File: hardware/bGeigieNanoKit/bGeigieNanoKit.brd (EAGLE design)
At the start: 57.1 x 73.7 mm, 5 parts

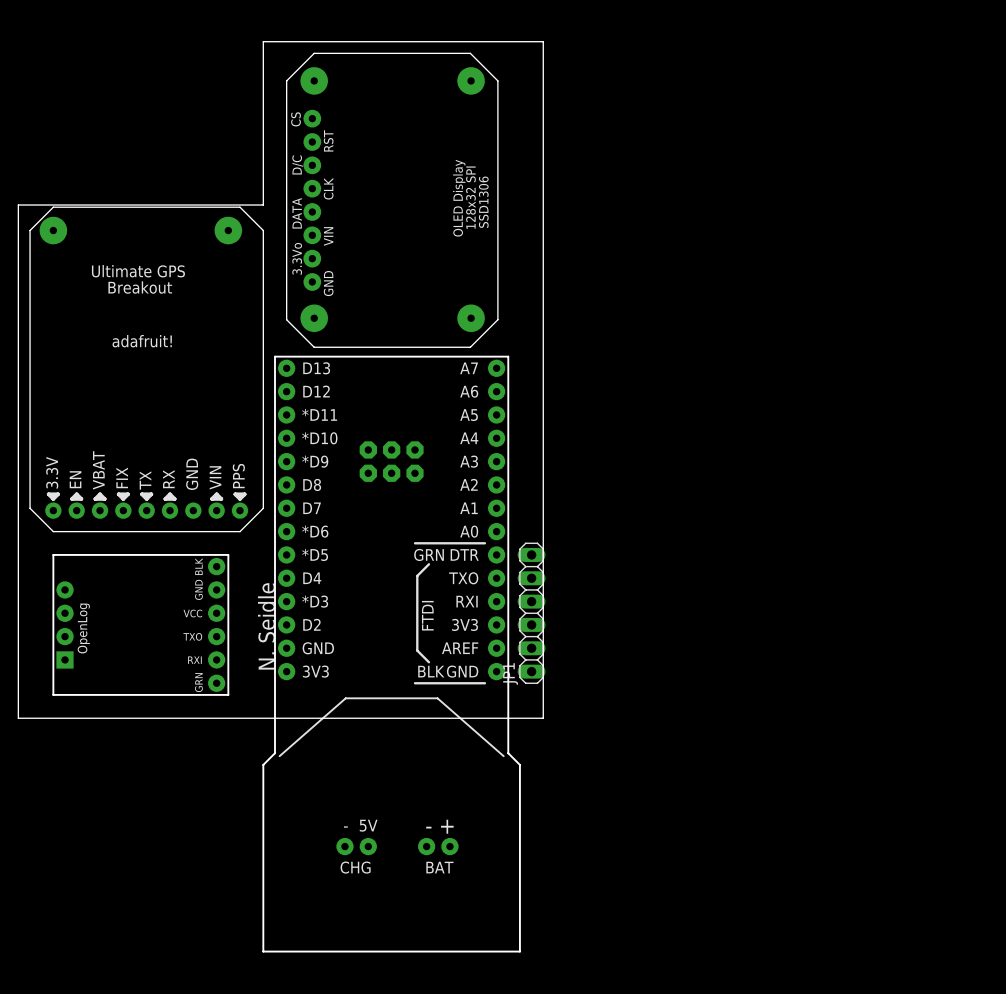
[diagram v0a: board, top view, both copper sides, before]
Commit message: library updated with full module footprints. test components removed. board updated to use new library components.
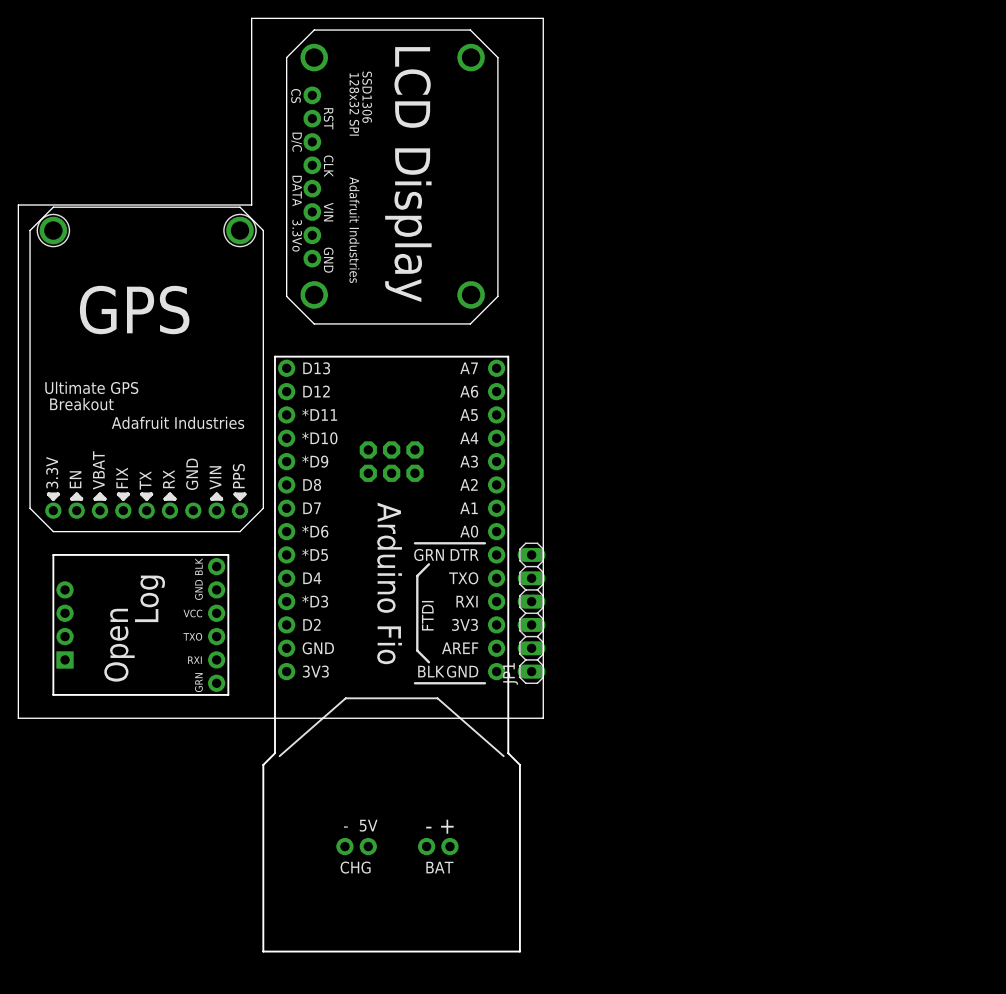
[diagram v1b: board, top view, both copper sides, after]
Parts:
- U$1: value OPENLOGTEST -> OPENLOG; device open_hw_sockets:TEST_OPENLOG -> open_hw_sockets:OPENLOG
- U$2: value FIO_SOCKETTEST -> FIO_SOCKET; device open_hw_sockets:TEST_FIO -> open_hw_sockets:FIO_V23_SOCKET
- U$3: value ULTIMATE_GPSTEST -> ULTIMATE_GPS; device open_hw_sockets:TEST_GPS -> open_hw_sockets:ULTIMATE_GPS_V3
- U$4: value LCD_SOCKETTEST -> SSD1306_128X32_SPI_LCD; device open_hw_sockets:TEST_LCD -> open_hw_sockets:SSD1306_128X32_SPI_LCD
- moved U$4 2.54 mm to (29.2, 100.3)
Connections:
- net GND: now also U$1.JP1$1, U$1.JP1$2, U$3.JP1$3, U$3.U$8$P$1, U$3.U$9$P$1, U$4.JP1$8, U$4.U$2$P$1, U$4.U$3$P$1, U$4.U$4$P$1, U$4.U$5$P$1; no longer U$1.JP1$5, U$1.JP1$6, U$3.JP1$2, U$3.U$8, U$3.U$9, U$4.8, U$4.U$2, U$4.U$3, U$4.U$4, U$4.U$5
- net N$1: now also U$1.JP1$6; no longer U$1.JP1$1
- net N$10: now also U$4.JP1$1; no longer U$4.1
- net N$2: now also U$1.JP1$5; no longer U$1.JP1$2
- net N$3: now also U$1.JP1$4; no longer U$1.JP1$3
- net N$4: now also U$3.JP1$4; no longer U$3.JP1$3
- net N$5: now also U$3.JP1$5; no longer U$3.JP1$4
- net N$6: now also U$4.JP1$5; no longer U$4.5
- net N$7: now also U$4.JP1$4; no longer U$4.4
- net N$8: now also U$4.JP1$3; no longer U$4.3
- net N$9: now also U$4.JP1$2; no longer U$4.2
- net VBAT: now also U$3.JP1$7; no longer U$3.JP1$6
- net VCC: now also U$1.JP1$3, U$3.JP1$9, U$4.JP1$7; no longer U$1.JP1$4, U$3.JP1$8, U$4.7
- net VIN: now also U$3.JP1$2, U$4.JP1$6; no longer U$3.JP1$1, U$4.6
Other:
- board size 57.1 x 73.7 mm -> 57.1 x 76.2 mm

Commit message: updated library footprints with single/double sided options. preliminary component placement on board to verify fit.
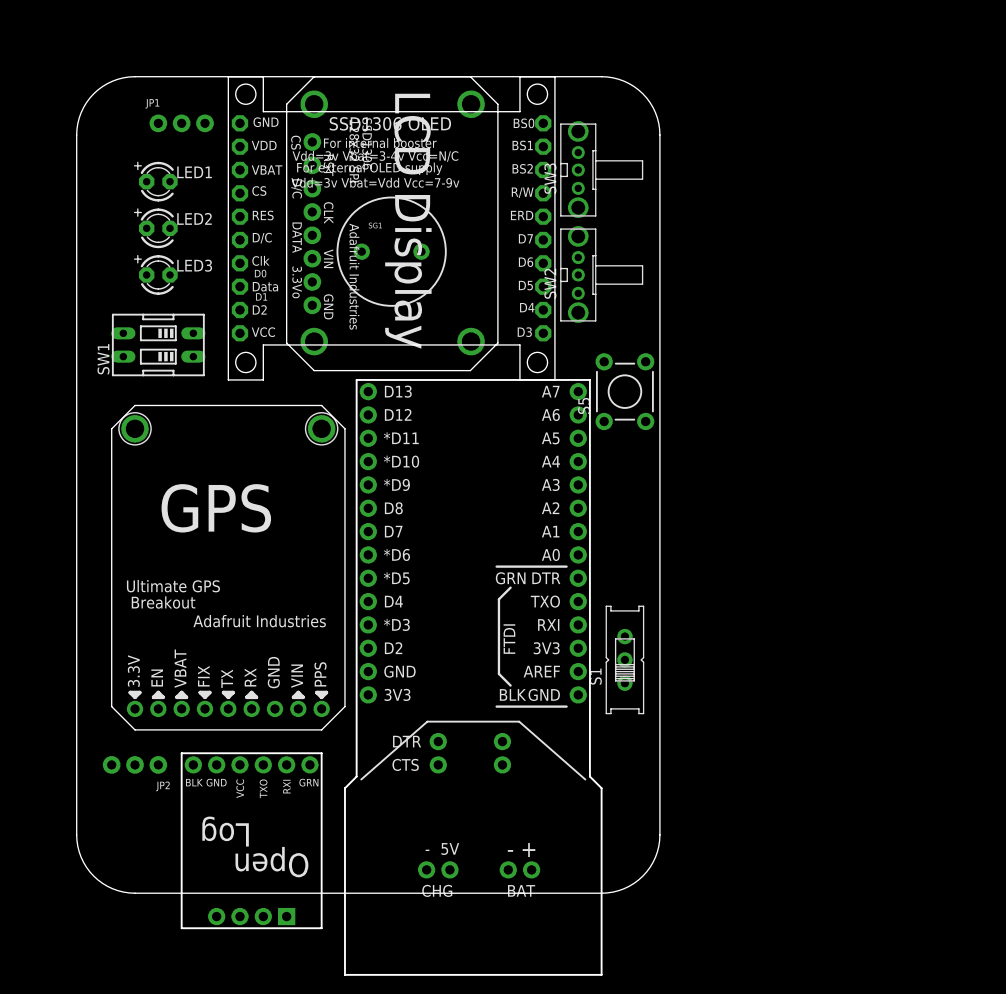
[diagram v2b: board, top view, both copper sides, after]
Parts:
- added JP2: (no value), microbuilder:1X03_ROUND_76
- added LED1, LED2, LED3: (no value), adafruit:LED3MM
- added S1: (no value), adafruit:EG1218
- added S5: (no value), SparkFun:TACTILE-PTH
- added SG1: BUZZERPTH, SparkFun:BUZZER-12MM
- added SW1: (no value), SparkFun:DIPSWITCH-02
- added SW2, SW3: OS102011MA1Q, adafruit:OS102011MA1Q
- added U$5: SSD1306_128X64_LCDTOP, open_hw_sockets:SSD1306_128X64_LCD_TOP
- JP1: device pinhead:1X06 -> microbuilder:1X03_ROUND_76
- U$2: value FIO_SOCKET -> FIO; device open_hw_sockets:FIO_V23_SOCKET -> open_hw_sockets:FIO_SOCKET
- U$3: value ULTIMATE_GPS -> GPS
- U$4: value SSD1306_128X32_SPI_LCD -> LCD
- moved JP1 65.5 mm to (17.8, 90.2), turned to 0 degrees
- moved U$3 23.3 mm to (10.2, 24.1)
- moved U$1 12.0 mm to (33.0, 21.6), turned to 180 degrees
- moved U$2 9.25 mm to (36.8, 62.2)
- moved U$4 5.08 mm to (29.2, 95.2)
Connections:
- removed net N$1: U$1.JP1$6, U$2.JP1$13
- removed net N$10: U$2.JP1$5, U$4.JP1$1
- removed net N$11: JP1.1, U$2.JP5$1
- removed net N$12: JP1.2, U$2.JP5$2
- removed net N$13: JP1.3, U$2.JP5$3
- removed net N$14: JP1.4, U$2.JP5$4
- removed net N$15: JP1.5, U$2.JP5$5
- removed net N$16: JP1.6, U$2.JP5$6
- removed net N$2: U$1.JP1$5, U$2.JP1$12
- removed net N$3: U$1.JP1$4, U$2.JP1$11
- removed net N$4: U$2.JP1$10, U$3.JP1$4
- removed net N$5: U$2.JP1$9, U$3.JP1$5
- removed net N$6: U$2.JP1$7, U$4.JP1$5
- removed net N$7: U$2.JP1$8, U$4.JP1$4
- removed net N$8: U$2.JP1$6, U$4.JP1$3
- removed net N$9: U$2.JP1$4, U$4.JP1$2
- new net 3.3V: U$3.JP1$9, U$4.JP1$7
- new net 3V3: U$2.JP1$1, U$2.JP5$3
- new net VDD: U$5.P0\$2
- net GND: now also U$2.JP5$1, U$5.P0\$1
- net VBAT: now also U$5.P0\$3
- net VCC: now also U$5.P0\$10; no longer U$2.JP1$1, U$3.JP1$9, U$4.JP1$7
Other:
- board size 57.1 x 76.2 mm -> 63.5 x 88.9 mm

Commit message: full set of components added to library. initital placement of all components.
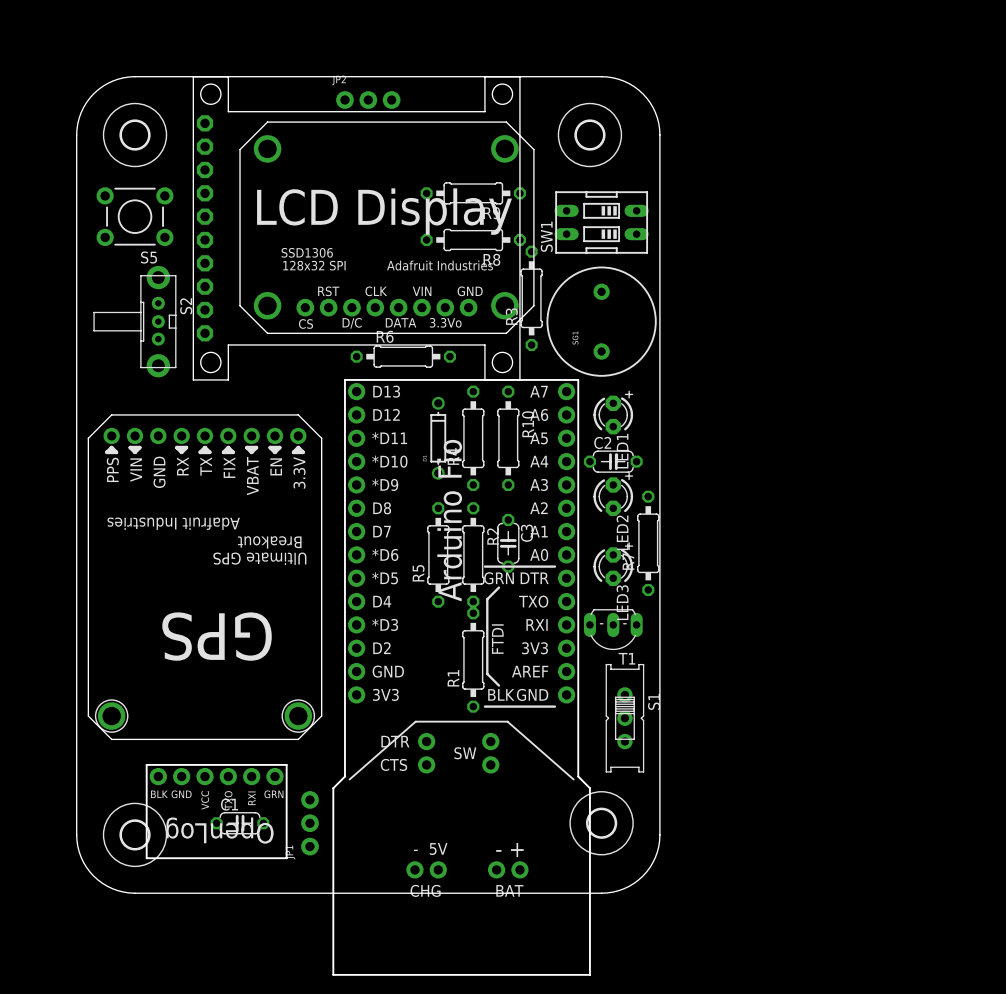
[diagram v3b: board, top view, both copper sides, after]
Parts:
- removed SW2, SW3: OS102011MA1Q, adafruit:OS102011MA1Q
- added C1, C2, C3: (no value), rcl:C050-024X044
- added D1: (no value), adafruit:DO-1N4148
- added H1, H2, H3, H4: MOUNT-HOLE3.0, holes:3,0
- added R1, R10, R2, R3, R4, R5, R6, R7, R8, R9: (no value), rcl:0207/10
- added S2: EG1213, adafruit:EG1213
- added T1: 2SC1815, transistor:TO92-ECB
- LED2: value (none) -> RED
- U$1: value OPENLOG -> OPENLOG_MIN; device open_hw_sockets:OPENLOG -> open_hw_sockets:OPENLOG_MIN
- U$2: value FIO -> FIO_SOCKETBOT; device open_hw_sockets:FIO_SOCKET -> open_hw_sockets:FIO_V23_SOCKET_BOT
- U$5: value SSD1306_128X64_LCDTOP -> SSD1306_128X64_LCD_MIN; device open_hw_sockets:SSD1306_128X64_LCD_TOP -> open_hw_sockets:SSD1306_128X64_LCD_MIN
- moved JP1 77.5 mm to (31.8, 14.0), turned to 90 degrees
- moved JP2 76.7 mm to (38.1, 92.7), turned to 0 degrees
- moved LED3 58.8 mm to (64.8, 41.9), turned to 270 degrees
- moved LED2 57.5 mm to (64.8, 49.5), turned to 270 degrees
- moved S5 56.6 mm to (12.7, 80.0), turned to 180 degrees
- moved LED1 55.7 mm to (64.8, 58.4), turned to 270 degrees
- moved SW1 50.1 mm to (63.5, 79.4)
- moved U$3 41.2 mm to (33.0, 58.4), turned to 180 degrees
- moved U$4 28.4 mm to (24.1, 67.3), turned to 0 degrees
- moved SG1 24.1 mm to (63.5, 68.6), turned to 90 degrees
- moved S1 6.35 mm to (66.0, 25.4), turned to 270 degrees
- moved U$1 4.02 mm to (29.2, 20.3)
- moved U$5 3.81 mm to (19.1, 66.0)
- moved U$2 1.27 mm to (35.6, 62.2)
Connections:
- removed net 3V3: U$2.JP1$1, U$2.JP5$3
- removed net VDD: U$5.P0\$2
- new net N$1: U$2.JP1$10, U$4.JP1$5, U$5.P0\$3
- new net N$10: U$1.JP1$1, U$2.JP1$5
- new net N$11: R1.2, R2.2, U$2.JP5$7
- new net N$12: S1.S, U$2.JP7$2
- new net N$13: S1.P, U$2.JP7$1
- new net N$14: R3.1, S2.2, U$2.JP5$14
- new net N$15: R4.1, U$2.JP5$8
- new net N$16: R4.2, SW1.4
- new net N$17: LED2.A, SW1.1
- new net N$18: C3.2, JP1.2, R5.1, U$2.JP1$3
- new net N$19: LED3.A, R7.1
- new net N$2: U$2.JP1$11, U$4.JP1$4, U$5.P0\$4
- new net N$20: S5.1, U$2.JP1$4
- new net N$21: R7.2, SG1.+, SW1.2
- new net N$22: LED3.K, T1.C
- new net N$23: R10.1, SG1.-
- new net N$24: C3.1, R10.2, R8.2
- new net N$25: JP2.1, R8.1, R9.1
- new net N$26: D1.A, R5.2
- new net N$27: C2.1, D1.C, R6.1
- new net N$28: R6.2, T1.B
- new net N$3: U$2.JP1$12, U$4.JP1$3, U$5.P0\$5
- new net N$4: U$2.JP1$13, U$4.JP1$1, U$5.P0\$7
- new net N$5: U$2.JP1$14, U$4.JP1$2, U$5.P0\$6
- new net N$6: U$2.JP1$9, U$3.JP1$5
- new net N$7: U$2.JP1$8, U$3.JP1$4
- new net N$8: U$1.JP1$3, U$2.JP1$7
- new net N$9: U$1.JP1$2, U$2.JP1$6
- new net VBATT: R1.1, U$2.JP2$2
- net GND: now also C1.1, C2.2, JP1.1, JP2.3, LED2.K, R2.1, R9.2, S2.3, S2.MT1, S2.MT2, S5.3, T1.E, U$1.JP1$5, U$1.JP1$6, U$2.JP2$1, U$2.JP6$1, U$5.P0\$10; no longer U$1.JP1$1, U$1.JP1$2, U$5.P0\$1
- net VBAT: no longer U$5.P0\$3
- net VCC: now also C1.2, JP1.3, R3.2, SW1.3, U$1.JP1$4, U$2.JP1$1, U$2.JP5$3, U$3.JP1$2, U$4.JP1$6, U$5.P0\$1, U$5.P0\$8, U$5.P0\$9; no longer U$1.JP1$3, U$5.P0\$10
- net VIN: now also U$2.JP6$2; no longer U$3.JP1$2, U$4.JP1$6

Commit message: resize board to be better fit in case. did inital pass at routing.
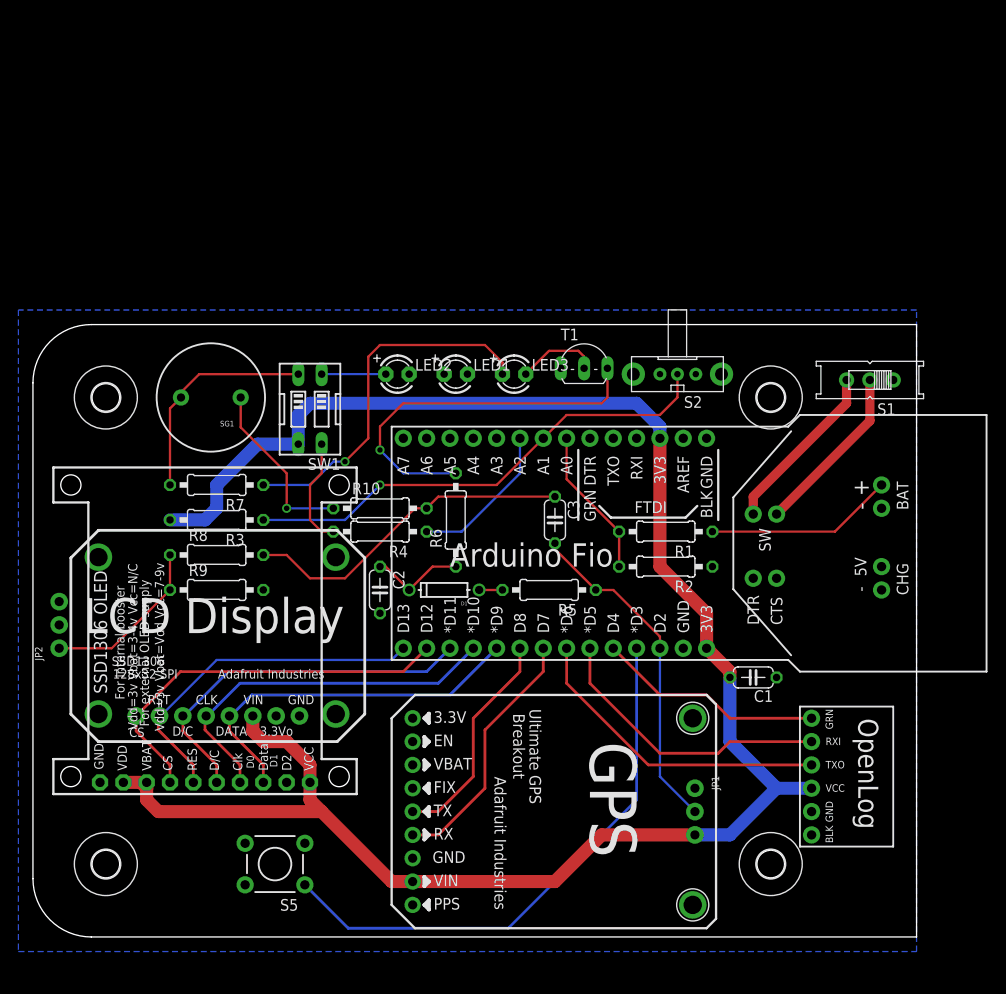
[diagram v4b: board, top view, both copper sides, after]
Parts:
- moved H3 79.4 mm to (9.53, 9.53), turned to 90 degrees
- moved S5 72.1 mm to (27.9, 9.53)
- moved H1 69.3 mm to (81.9, 9.53), turned to 90 degrees
- moved JP2 66.3 mm to (4.45, 35.6), turned to 90 degrees
- moved H2 60.0 mm to (9.53, 60.3), turned to 90 degrees
- moved C1 58.1 mm to (80.0, 29.8), turned to 180 degrees
- moved S2 56.8 mm to (71.8, 62.9), turned to 180 degrees
- moved U$1 56.2 mm to (85.1, 26.7), turned to 270 degrees
- moved R9 51.4 mm to (21.6, 39.4), turned to 0 degrees
- moved U$5 50.9 mm to (33.0, 17.1), turned to 90 degrees
- moved H4 49.9 mm to (81.9, 60.3), turned to 90 degrees
- moved U$4 48.1 mm to (5.71, 22.9)
- moved R7 47.4 mm to (21.6, 50.8), turned to 180 degrees
- moved S1 45.5 mm to (92.7, 62.2), turned to 180 degrees
- moved R8 44.2 mm to (21.6, 43.2), turned to 0 degrees
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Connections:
- removed net 3.3V: U$3.JP1$9, U$4.JP1$7
- net N$12: now also S1.P; no longer S1.S
- net N$13: now also S1.S; no longer S1.P
- net N$14: now also U$2.JP5$8; no longer U$2.JP5$14
- net N$15: now also U$2.JP5$9; no longer U$2.JP5$8
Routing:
- net VCC: track 0.00 -> 207.6 mm
- net N$20: track 0.00 -> 60.4 mm
- net N$14: track 0.00 -> 53.1 mm, vias 0 -> 1
- net N$4: track 0.00 -> 43.4 mm
- net N$28: track 0.00 -> 41.1 mm, vias 0 -> 1
- net N$2: track 0.00 -> 41.0 mm
- net N$3: track 0.00 -> 40.9 mm
- net N$1: track 0.00 -> 40.9 mm
- net N$19: track 0.00 -> 39.6 mm, vias 0 -> 1
- net N$5: track 0.00 -> 38.5 mm
- net N$18: track 0.00 -> 36.6 mm
- net N$24: track 0.00 -> 36.5 mm
- net N$8: track 0.00 -> 34.2 mm
- net N$9: track 0.00 -> 31.6 mm
- net N$7: track 0.00 -> 27.8 mm
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- added copper zone on layer 16, net GND
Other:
- board size 63.5 x 88.9 mm -> 96.2 x 66.7 mm

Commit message: fully routed board
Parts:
- removed H1, H2, H3, H4: MOUNT-HOLE3.0, holes:3,0
- removed LED3: (no value), adafruit:LED3MM
- removed S2: EG1213, adafruit:EG1213
- added S3: (no value), adafruit:EG1218
- added U$6, U$7, U$8, U$9: MOUNTINGHOLE3.0THIN, microbuilder:MOUNTINGHOLE_3.0_PLATEDTHIN
- SW1: device SparkFun:DIPSWITCH-02 -> special:EDG-02
- moved S1 35.6 mm to (91.4, 26.7)
- moved R10 17.9 mm to (21.6, 46.4)
- moved C3 12.7 mm to (45.7, 47.6), turned to 0 degrees
- moved R6 12.1 mm to (47.0, 59.1), turned to 0 degrees
- moved LED1 6.48 mm to (54.0, 64.1)
- moved U$1 5.24 mm to (86.4, 21.6)
- moved JP2 4.49 mm to (3.81, 31.1)
- moved LED2 4.02 mm to (45.1, 64.1)
- moved R4 4.02 mm to (43.2, 44.5)
- moved R3 2.54 mm to (21.6, 49.5), turned to 0 degrees
- moved SW1 2.29 mm to (33.0, 61.0)
- moved R7 1.91 mm to (21.6, 52.7), turned to 0 degrees
- moved S5 1.27 mm to (27.9, 10.8), turned to 0 degrees
- moved R9 0.64 mm to (21.6, 40.0)
- moved T1 0.64 mm to (61.6, 64.1), turned to 180 degrees
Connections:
- net GND: now also S3.S; no longer S2.3, S2.MT1, S2.MT2
- net N$14: now also S3.P, U$2.JP5$14; no longer S2.2, U$2.JP5$8
- net N$19: now also LED1.A, R7.2; no longer LED3.A, R7.1
- net N$21: now also R7.1; no longer R7.2
- net N$22: now also LED1.K; no longer LED3.K
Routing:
- net N$28: track 41.1 -> 9.09 mm, vias 1 -> 0
- net N$24: track 36.5 -> 20.2 mm
- net N$27: track 10.4 -> 22.4 mm
- net N$18: track 36.6 -> 47.7 mm
- net N$14: track 53.1 -> 43.9 mm, vias 1 -> 0
- net VCC: track 207.6 -> 216.5 mm
- net N$19: track 39.6 -> 31.5 mm, vias 1 -> 0
- net N$13: track 18.8 -> 26.1 mm
- net N$12: track 18.8 -> 25.8 mm
- net N$20: track 60.4 -> 54.6 mm
- net N$10: track 24.7 -> 28.1 mm
- net N$25: track 18.5 -> 21.7 mm
- net N$16: track 6.98 -> 9.79 mm
- net N$15: track 16.6 -> 14.1 mm
- net N$17: track 11.8 -> 14.3 mm
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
